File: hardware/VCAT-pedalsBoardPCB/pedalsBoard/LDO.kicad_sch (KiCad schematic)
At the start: 5 parts, among them U5 MCP1826S

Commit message: monday evening check
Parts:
- renumbered C30 to C46, C31 to C47, D5 to D10, TP_3.3V1 to TP_3.3V2, U5 to U7
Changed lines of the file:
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@@
 		(dnp no)
 		(fields_autoplaced yes)
-		(property "Reference" "C31"
+		(property "Reference" "C47"
 			(at 168.275 68.5735 0)
 			(show_name no)
@@
 		(instances
 			(project "pedalsBoard"
-				(path "/423853f6-a5c6-4d97-9a9a-db6f143664c7/765862e6-177a-45ce-82fa-2a064b9bcb00"
-					(reference "C31")
-					(unit 1)
-				)
-			)
-			(project "LDO"
-				(path "/8ff43370-8d10-4d2c-b1a3-81d1c2934a98"
-					(reference "C2")
-					(unit 1)
-				)
-			)
-			(project "LeaderSOMBreakout"
-				(path "/e5b32072-3e3d-42a6-9d41-1a76d538e329/f3053c74-1ac6-4a33-80f3-565e8c4c2c7d"
-					(reference "C?")
+				(path "/423853f6-a5c6-4d97-9a9a-db6f143664c7/26d9f075-73a6-4044-b4f9-8fe225c47fcc/9b03dc66-1214-42b2-8747-33b789bdecf9"
+					(reference "C47")
 					(unit 1)
 				)
@@
 		(in_pos_files yes)
 		(dnp no)
-		(property "Reference" "TP_3.3V1"
+		(property "Reference" "TP_3.3V2"
 			(at 166.624 54.356 90)
 			(show_name no)
@@
 		(instances
 			(project "pedalsBoard"
-				(path "/423853f6-a5c6-4d97-9a9a-db6f143664c7/765862e6-177a-45ce-82fa-2a064b9bcb00"
-					(reference "TP_3.3V1")
-					(unit 1)
-				)
-			)
-			(project "LDO"
-				(path "/8ff43370-8d10-4d2c-b1a3-81d1c2934a98"
-					(reference "TP_3.3V1")
+				(path "/423853f6-a5c6-4d97-9a9a-db6f143664c7/26d9f075-73a6-4044-b4f9-8fe225c47fcc/9b03dc66-1214-42b2-8747-33b789bdecf9"
+					(reference "TP_3.3V2")
 					(unit 1)
 				)
@@
 		(dnp no)
 		(fields_autoplaced yes)
-		(property "Reference" "U5"
+		(property "Reference" "U7"
 			(at 152.4 56.515 0)
 			(show_name no)
@@
 		(instances
 			(project "pedalsBoard"
-				(path "/423853f6-a5c6-4d97-9a9a-db6f143664c7/765862e6-177a-45ce-82fa-2a064b9bcb00"
-					(reference "U5")
-					(unit 1)
-				)
-			)
-			(project ""
-				(path "/8ff43370-8d10-4d2c-b1a3-81d1c2934a98"
-					(reference "U1")
+				(path "/423853f6-a5c6-4d97-9a9a-db6f143664c7/26d9f075-73a6-4044-b4f9-8fe225c47fcc/9b03dc66-1214-42b2-8747-33b789bdecf9"
+					(reference "U7")
 					(unit 1)
 				)
@@
 		(dnp no)
 		(fields_autoplaced yes)
-		(property "Reference" "D5"
+		(property "Reference" "D10"
 			(at 133.604 57.15 0)
 			(show_name no)
@@
 		(instances
 			(project "pedalsBoard"
-				(path "/423853f6-a5c6-4d97-9a9a-db6f143664c7/765862e6-177a-45ce-82fa-2a064b9bcb00"
-					(reference "D5")
-					(unit 1)
-				)
-			)
-			(project ""
-				(path "/8ff43370-8d10-4d2c-b1a3-81d1c2934a98"
-					(reference "D1")
+				(path "/423853f6-a5c6-4d97-9a9a-db6f143664c7/26d9f075-73a6-4044-b4f9-8fe225c47fcc/9b03dc66-1214-42b2-8747-33b789bdecf9"
+					(reference "D10")
 					(unit 1)
 				)
@@
 		(dnp no)
 		(fields_autoplaced yes)
-		(property "Reference" "C30"
+		(property "Reference" "C46"
 			(at 142.875 68.5735 0)
 			(show_name no)
@@
 		(instances
 			(project "pedalsBoard"
-				(path "/423853f6-a5c6-4d97-9a9a-db6f143664c7/765862e6-177a-45ce-82fa-2a064b9bcb00"
-					(reference "C30")
+				(path "/423853f6-a5c6-4d97-9a9a-db6f143664c7/26d9f075-73a6-4044-b4f9-8fe225c47fcc/9b03dc66-1214-42b2-8747-33b789bdecf9"
+					(reference "C46")
 					(unit 1)
 				)
-			)
-			(project "LDO"
-				(path "/8ff43370-8d10-4d2c-b1a3-81d1c2934a98"
-					(reference "C1")
-					(unit 1)
-				)
-			)
-			(project ""
-				(path "/e5b32072-3e3d-42a6-9d41-1a76d538e329/f3053c74-1ac6-4a33-80f3-565e8c4c2c7d"
-					(reference "C?")
-					(unit 1)
-				)

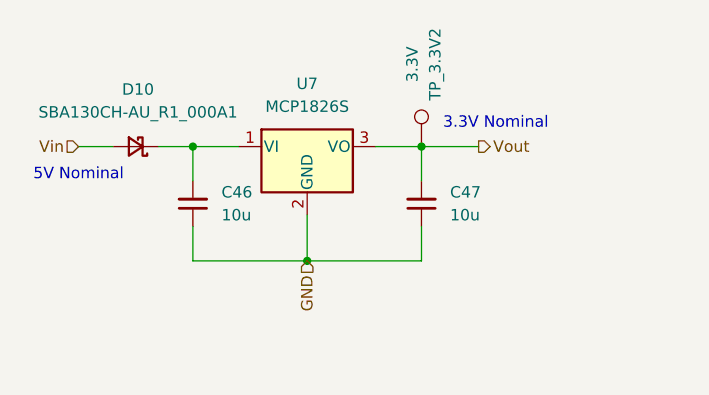
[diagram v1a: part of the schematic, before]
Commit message: addressed review, brake switch on slack
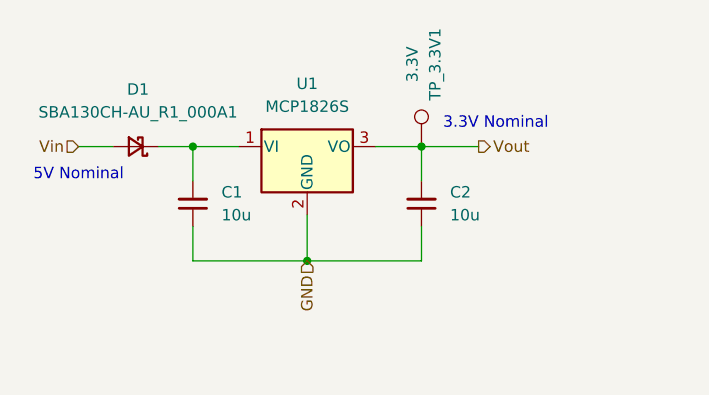
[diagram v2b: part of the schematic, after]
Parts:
- renumbered C46 to C1, C47 to C2, D10 to D1, TP_3.3V2 to TP_3.3V1, U7 to U1
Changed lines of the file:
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@@
 		(dnp no)
 		(fields_autoplaced yes)
-		(property "Reference" "C47"
+		(property "Reference" "C2"
 			(at 168.275 68.5735 0)
 			(show_name no)
@@
 		(instances
 			(project "pedalsBoard"
-				(path "/423853f6-a5c6-4d97-9a9a-db6f143664c7/26d9f075-73a6-4044-b4f9-8fe225c47fcc/9b03dc66-1214-42b2-8747-33b789bdecf9"
-					(reference "C47")
+				(path "/423853f6-a5c6-4d97-9a9a-db6f143664c7/26d9f075-73a6-4044-b4f9-8fe225c47fcc/5b9f2d54-3176-493c-bd56-b8351d5c1c1f"
+					(reference "C2")
 					(unit 1)
 				)
@@
 		(in_pos_files yes)
 		(dnp no)
-		(property "Reference" "TP_3.3V2"
+		(property "Reference" "TP_3.3V1"
 			(at 166.624 54.356 90)
 			(show_name no)
@@
 		(instances
 			(project "pedalsBoard"
-				(path "/423853f6-a5c6-4d97-9a9a-db6f143664c7/26d9f075-73a6-4044-b4f9-8fe225c47fcc/9b03dc66-1214-42b2-8747-33b789bdecf9"
-					(reference "TP_3.3V2")
+				(path "/423853f6-a5c6-4d97-9a9a-db6f143664c7/26d9f075-73a6-4044-b4f9-8fe225c47fcc/5b9f2d54-3176-493c-bd56-b8351d5c1c1f"
+					(reference "TP_3.3V1")
 					(unit 1)
 				)
@@
 		(dnp no)
 		(fields_autoplaced yes)
-		(property "Reference" "U7"
+		(property "Reference" "U1"
 			(at 152.4 56.515 0)
 			(show_name no)
@@
 		(instances
 			(project "pedalsBoard"
-				(path "/423853f6-a5c6-4d97-9a9a-db6f143664c7/26d9f075-73a6-4044-b4f9-8fe225c47fcc/9b03dc66-1214-42b2-8747-33b789bdecf9"
-					(reference "U7")
+				(path "/423853f6-a5c6-4d97-9a9a-db6f143664c7/26d9f075-73a6-4044-b4f9-8fe225c47fcc/5b9f2d54-3176-493c-bd56-b8351d5c1c1f"
+					(reference "U1")
 					(unit 1)
 				)
@@
 		(dnp no)
 		(fields_autoplaced yes)
-		(property "Reference" "D10"
+		(property "Reference" "D1"
 			(at 133.604 57.15 0)
 			(show_name no)
@@
 		(instances
 			(project "pedalsBoard"
-				(path "/423853f6-a5c6-4d97-9a9a-db6f143664c7/26d9f075-73a6-4044-b4f9-8fe225c47fcc/9b03dc66-1214-42b2-8747-33b789bdecf9"
-					(reference "D10")
+				(path "/423853f6-a5c6-4d97-9a9a-db6f143664c7/26d9f075-73a6-4044-b4f9-8fe225c47fcc/5b9f2d54-3176-493c-bd56-b8351d5c1c1f"
+					(reference "D1")
 					(unit 1)
 				)
@@
 		(dnp no)
 		(fields_autoplaced yes)
-		(property "Reference" "C46"
+		(property "Reference" "C1"
 			(at 142.875 68.5735 0)
 			(show_name no)
@@
 		(instances
 			(project "pedalsBoard"
-				(path "/423853f6-a5c6-4d97-9a9a-db6f143664c7/26d9f075-73a6-4044-b4f9-8fe225c47fcc/9b03dc66-1214-42b2-8747-33b789bdecf9"
-					(reference "C46")
+				(path "/423853f6-a5c6-4d97-9a9a-db6f143664c7/26d9f075-73a6-4044-b4f9-8fe225c47fcc/5b9f2d54-3176-493c-bd56-b8351d5c1c1f"
+					(reference "C1")
 					(unit 1)
 				)

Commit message: hopefully final before layout
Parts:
- TP_3.3V1: footprint TestPoint:TestPoint_Loop_D1.80mm_Drill1.0mm_Beaded -> LHRS_Special:TestPoint_HEX_3mmID
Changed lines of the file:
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@@
 			)
 		)
-		(property "Footprint" "TestPoint:TestPoint_Loop_D1.80mm_Drill1.0mm_Beaded"
+		(property "Footprint" "LHRS_Special:TestPoint_HEX_3mmID"
 			(at 170.18 63.5 0)
 			(hide yes)
